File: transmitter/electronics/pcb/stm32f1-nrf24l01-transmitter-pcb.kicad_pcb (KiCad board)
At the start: 2 copper layers, 100 x 48 mm, 69 parts, among them J1 PA1/A1, J10 PB3, J11 PB4, J12 PB5, J13 PB6, J14 PB7, J15 PB8, J16 PB10, J17 PB11, J18 External charger LED, J19 BATTERY, J2 PA2/A2, J20 Red, J21 Blue, J22 POWER SWITCH, J23 USB, J24 UART, J25 SWD, J26 Buzzer, J27 NRF24 connector, J29 Meter, J3 PA3/A3, J30 LED, J4 PA4/A4, J5 PA5/A5, J6 PA6/A6, J7 PA7/A7, J8 PB0/A8, J9 PB1/A9, Q1 PMV30UN, SW1 RESET, U1 MCP1703A-3302, U2 LIPO_CHARGER_+_PROTECTION, U3 STM32F103CBT6, U4 MCP1703A-3302, Y1 8MHz

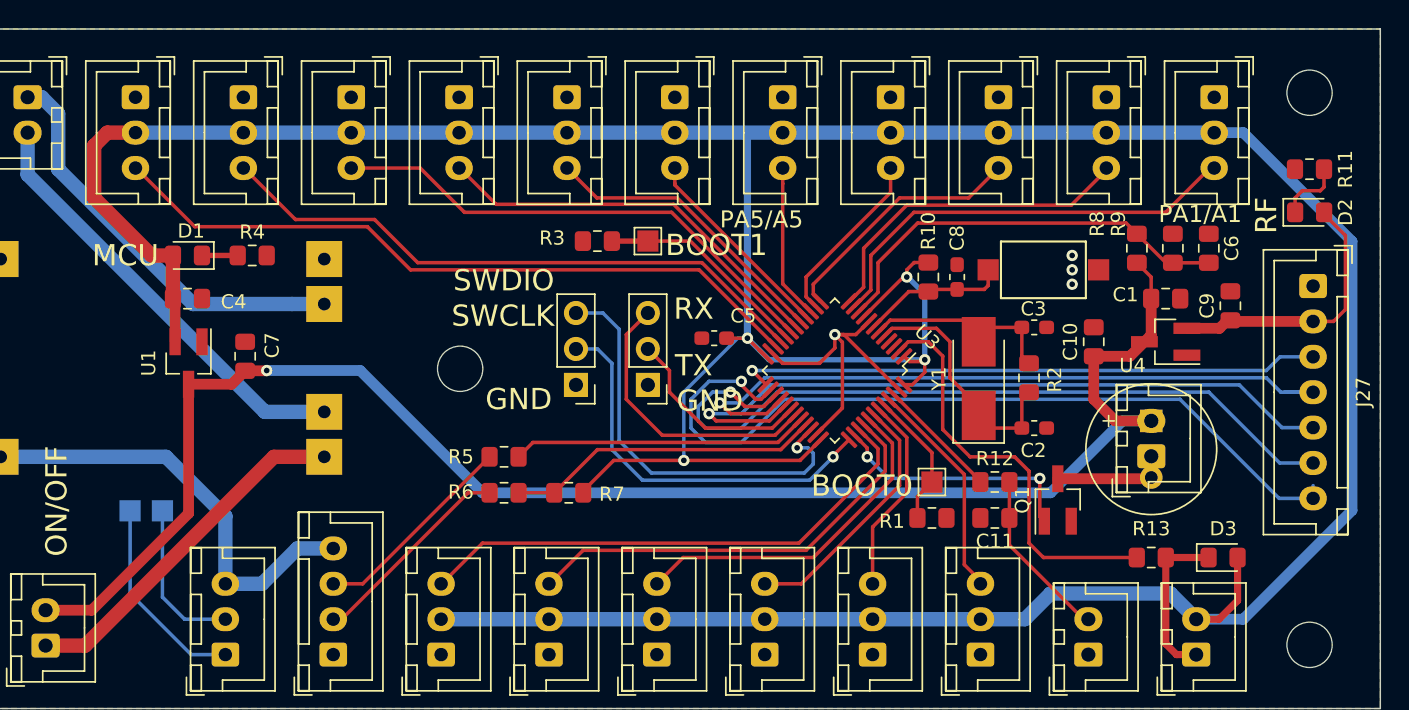
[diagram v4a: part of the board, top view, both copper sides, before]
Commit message: Revise layout
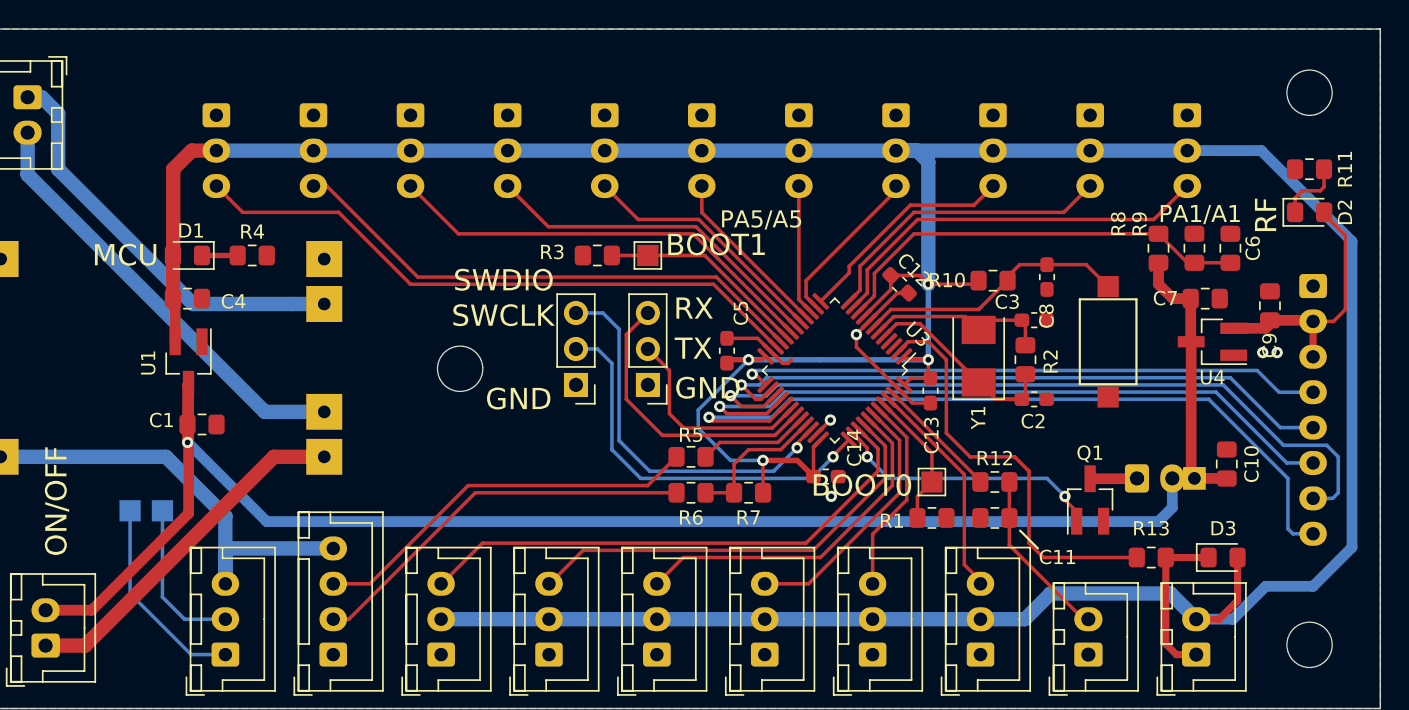
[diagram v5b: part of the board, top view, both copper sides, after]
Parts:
- added C12: 100n, Capacitor_SMD:C_0603_1608Metric_Pad1.05x0.95mm_HandSolder, F.Cu at (166.0, 70.0)
- added C13: 100n, Capacitor_SMD:C_0603_1608Metric_Pad1.05x0.95mm_HandSolder, F.Cu at (168.2, 77.5)
- added C14: 100n, Capacitor_SMD:C_0603_1608Metric_Pad1.05x0.95mm_HandSolder, F.Cu at (160.8, 83.6)
- J1, J16, J17, J2, J26, J3, J4, J5, J6, J7, J8, J9, SP1: moved to B.Cu
- J27: footprint Connector_JST:JST_XH_B7B-XH-A_1x07_P2.50mm_Vertical -> Connector_JST:JST_XH_B8B-XH-A_1x08_P2.50mm_Vertical; moved to B.Cu
- Y1: footprint Crystal:Crystal_SMD_5032-2Pin_5.0x3.2mm_HandSoldering -> Crystal:Crystal_SMD_5032-2Pin_5.0x3.2mm
- moved C1 68.7 mm to (116.8, 79.9)
- moved C7 67.9 mm to (187.6, 71.0), turned to 0 degrees
- moved R5 13.2 mm to (151.3, 82.2)
- moved R6 13.2 mm to (151.3, 84.8)
- moved C10 12.8 mm to (189.2, 82.7)
- moved R7 12.7 mm to (155.4, 84.8)
- moved SW1 6.83 mm to (180.8, 74.1), turned to 90 degrees
- moved C8 6.35 mm to (176.5, 69.5), turned to 270 degrees
- moved J17 5.85 mm to (117.8, 58.1)
- moved J16 5.11 mm to (124.6, 58.1)
- moved SP1 5.08 mm to (186.9, 83.7), turned to 180 degrees
- moved R10 4.58 mm to (172.6, 69.8), turned to 0 degrees
- moved J9 4.38 mm to (131.5, 58.1)
- moved J8 3.66 mm to (138.4, 58.1)
- moved U4 3.30 mm to (188.1, 74.1)
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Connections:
- J27 pad 3: /CSN -> /3V3_RF
- J27 pad 4: /MOSI -> /CSN
- J27 pad 5: /IRQ -> /SCK
- J27 pad 6: /MISO -> /MOSI
- J27 pad 7: /SCK -> /MISO
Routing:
- net +3V3: track 281.4 -> 263.9 mm
- net /SCK: track 58.9 -> 44.8 mm
- net /USBDM: track 21.0 -> 7.81 mm
- net Net-(J23-Pad2): track 14.7 -> 27.9 mm
- net Net-(J23-Pad3): track 14.8 -> 28.0 mm
- net /USBDP: track 22.3 -> 10.3 mm
- net /NRST: track 10.4 -> 19.1 mm
- net VDD: track 114.1 -> 122.1 mm
- net /PB11: track 50.4 -> 44.2 mm
- net /PB10: track 43.0 -> 37.5 mm
- net Net-(J26-Pad1): track 8.14 -> 3.38 mm
- net /PB1-ADC9: track 35.8 -> 31.1 mm
- net /IRQ: track 50.9 -> 55.2 mm
- net /PB0-ADC8: track 28.4 -> 24.5 mm
- net GND: track 23.3 -> 19.7 mm, vias 4 -> 5
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
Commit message: Make combined PCB
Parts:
- added H4: MountingHole, MountingHole:MountingHole_3.2mm_M3_DIN965, F.Cu at (140.0, 91.0)
- added H5: MountingHole, MountingHole:MountingHole_3.2mm_M3_DIN965, F.Cu at (140.0, 63.0)
- added H6: MountingHole, MountingHole:MountingHole_3.2mm_M3_DIN965, F.Cu at (195.0, 63.0)
- added H7: MountingHole, MountingHole:MountingHole_3.2mm_M3_DIN965, F.Cu at (195.0, 91.0)
- added H8: MountingHole, MountingHole:MountingHole_3.2mm_M3_DIN965, F.Cu at (100.0, 63.0)
- J10, J11, J12, J13, J14, J15, J18, J19, J22, J23, J29, J30: moved to B.Cu
- moved R7 41.8 mm to (114.7, 94.4)
- moved R5 38.6 mm to (112.7, 82.5)
- moved R6 38.6 mm to (112.7, 84.8)
- moved J18 34.7 mm to (83.7, 95.4), turned to 180 degrees
- moved R4 34.0 mm to (89.1, 81.5), turned to 270 degrees
- moved J20 33.1 mm to (81.2, 90.9)
- moved J16 32.4 mm to (92.6, 63.4)
- moved J17 32.4 mm to (85.8, 63.4)
- moved D1 28.3 mm to (89.1, 77.4), turned to 90 degrees
- moved J25 27.5 mm to (120.1, 92.1)
- moved J21 27.1 mm to (85.0, 90.9)
- moved J19 26.4 mm to (78.9, 63.4)
- moved TP2 25.4 mm to (123.0, 70.4), turned to 90 degrees
- moved U2 25.4 mm to (89.1, 80.2)
- moved R3 25.0 mm to (119.8, 70.4)
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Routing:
- net /USBDP: track 10.3 -> 42.0 mm
- net /USBDM: track 7.81 -> 32.7 mm
- net Net-(J23-Pad2): track 27.9 -> 10.4 mm
- net Net-(J23-Pad3): track 28.0 -> 10.9 mm
- net /PB11: track 44.2 -> 61.0 mm
- net /PB10: track 37.5 -> 54.3 mm
- net /METER: track 8.69 -> 24.1 mm
- net /PA2-ADC2: track 21.4 -> 36.2 mm
- net +3V3: track 263.9 -> 278.7 mm, vias 4 -> 1
- net /PA3-ADC3: track 15.8 -> 30.3 mm
- net /PA4-ADC4: track 11.4 -> 25.8 mm
- net /PB5: track 24.8 -> 10.4 mm
- net /PA1-ADC1: track 28.0 -> 42.4 mm
- net VDD: track 122.1 -> 134.8 mm, vias 1 -> 2
- net /PA5-ADC5: track 9.20 -> 20.1 mm
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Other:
- board size 100 x 48 mm -> 124 x 47 mm
- net class Default: clearance 0.2 -> 0.2032; trace_width 0.25 -> 0.254
- rule trace_clearance: 0.2 -> 0.2032
- rule trace_min: 0.2 -> 0.2032
- board text added: "+ DM DP GND"
- board text added: "- +"
- board text added: "3V3 MCU"
- board text added: "3V3 RF"
- board text added: "B+"
- board text added: "B-"
- board text added: "BAT"
- board text added: "BATTERY"
- board text added: "BUZZER"
- board text added: "CHARGER LED"
- board text added: "LED"
- board text added: "METER"
- board text added: "NRF24L01P"
- board text added: "OUT+"
- board text added: "OUT-"
- board text added: "PA2/A2"
- board text added: "PA3/A3"
- board text added: "PA4/A4"
- board text added: "PA6/A6"
- board text added: "PA7/A7"
- board text added: "PB0/A8"
- board text added: "PB1/A9"
- board text added: "PB10"
- board text added: "PB11"
- board text added: "PB3"
- board text added: "PB4"
- board text added: "PB5"
- board text added: "PB6"
- board text added: "PB7"
- board text added: "PB8"
- board text added: "RESET"
- board text added: "USB"
- board text removed: "MCU"
- board text removed: "RF"

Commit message: Finalize layout
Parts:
- added H10: MountingHole, MountingHole:MountingHole_3.2mm_M3_DIN965, F.Cu at (75.0, 56.5)
- added H9: MountingHole, MountingHole:MountingHole_3.2mm_M3_DIN965, F.Cu at (75.0, 95.5)
- H4, H5, H6, H7, H8: footprint MountingHole:MountingHole_3.2mm_M3_DIN965 -> MountingHole:MountingHole_2.7mm_M2.5_DIN965
- moved J9 35.1 mm to (90.9, 63.4)
- moved J19 28.7 mm to (103.0, 78.9)
- moved J22 28.4 mm to (103.0, 70.0), turned to 270 degrees
- moved R7 8.75 mm to (106.9, 90.6), turned to 0 degrees
- moved J16 8.64 mm to (84.0, 63.4)
- moved J17 8.64 mm to (77.1, 63.4)
- moved C1 7.27 mm to (92.1, 78.2), turned to 90 degrees
- moved J25 7.23 mm to (113.2, 89.8), turned to 90 degrees
- moved R5 6.84 mm to (106.9, 86.0)
- moved R6 6.84 mm to (106.9, 88.3)
- moved J23 6.78 mm to (102.0, 94.9), turned to 180 degrees
- moved D1 5.24 mm to (85.0, 74.1)
- moved U1 5.24 mm to (88.6, 77.6)
- moved R4 5.24 mm to (85.0, 78.2)
- moved C4 5.24 mm to (88.6, 73.1)
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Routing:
- net /PB1-ADC9: track 21.5 -> 57.2 mm
- net Net-(J19-Pad2): track 31.4 -> 7.67 mm
- net Net-(J19-Pad1): track 30.3 -> 7.66 mm
- net +3V3: track 278.7 -> 294.7 mm
- net /+USB: track 40.9 -> 25.9 mm
- net /RX: track 27.0 -> 14.9 mm
- net /PB10: track 54.3 -> 65.9 mm
- net /PB11: track 61.0 -> 72.6 mm
- net Net-(J22-Pad1): track 14.8 -> 25.0 mm
- net /USBDM: track 32.7 -> 38.3 mm
- net VDD: track 134.8 -> 129.5 mm
- net /SWDCLK: track 33.0 -> 38.1 mm
- net /TX: track 23.0 -> 18.0 mm
- net Net-(J23-Pad3): track 10.9 -> 14.5 mm
- net /SWDIO: track 26.3 -> 29.5 mm
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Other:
- board size 124 x 47 mm -> 128 x 47 mm
- net class Default: clearance 0.2032 -> 0.1524
- rule trace_clearance: 0.2032 -> 0.1524
- board text added: "+"
- board text added: "LANE Boys RC"

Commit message: Add JLC fabrication marker
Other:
- board text added: "JLCJLCJLCJLC"
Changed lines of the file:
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@@
   (general
     (thickness 1.6)
-    (drawings 99)
+    (drawings 100)
     (tracks 406)
     (zones 0)
@@
   )
   (setup
-    (last_trace_width 0.381)
+    (last_trace_width 0.254)
     (user_trace_width 0.381)
     (user_trace_width 0.508)
@@
     (pad_drill 3.2)
     (pad_to_mask_clearance 0)
-    (aux_axis_origin 100 100)
-    (grid_origin 100 100)
+    (aux_axis_origin 71 100)
+    (grid_origin 71 100)
     (visible_elements FFFFFF7F)
     (pcbplotparams
@@
     )
   )
+  (gr_text JLCJLCJLCJLC (at 73.584 80.188 90) (layer B.SilkS)
+    (effects (font (size 0.8 0.8) (thickness 0.15)) (justify mirror))
+  )
   (gr_text + (at 191.948 81.458 90) (layer F.SilkS)
     (effects (font (size 1.5 1.5) (thickness 0.3)) (justify left))
@@
   (segment (start 99.532 94.92) (end 99.532 90.054) (width 0.254) (layer F.Cu) (net 36))
   (segment (start 99.532 90.054) (end 101.27 88.316) (width 0.254) (layer F.Cu) (net 36))
+  (segment (start 105.851 88.0575) (end 105.851 88.316) (width 0.254) (layer F.Cu) (net 36))
+  (segment (start 103.801 88.316) (end 105.833 88.316) (width 0.254) (layer F.Cu) (net 36))
   (segment (start 131.496 84.506) (end 130.48 83.49) (width 0.254) (layer F.Cu) (net 37) (status 20))
   (segment (start 144.223445 82.800109) (end 142.517554 84.506) (width 0.254) (layer F.Cu) (net 37) (status 10))
@@
   (segment (start 145.284105 83.860769) (end 143.114874 86.03) (width 0.254) (layer F.Cu) (net 39) (status 10))
   (segment (start 143.114874 86.03) (end 122.098 86.03) (width 0.254) (layer F.Cu) (net 39))
+  (segment (start 117.272 91.364) (end 115.748 89.84) (width 0.254) (layer F.Cu) (net 40))
+  (segment (start 119.05 91.364) (end 117.272 91.364) (width 0.254) (layer F.Cu) (net 40))
+  (segment (start 123.876 86.538) (end 119.05 91.364) (width 0.254) (layer F.Cu) (net 40))
+  (segment (start 147.498 85.058664) (end 147.498 87.3) (width 0.254) (layer F.Cu) (net 40))
+  (segment (start 142.926 86.538) (end 123.876 86.538) (width 0.254) (layer F.Cu) (net 40))
+  (segment (start 147.988788 84.567876) (end 147.498 85.058664) (width 0.254) (layer F.Cu) (net 40))
+  (segment (start 147.498 87.3) (end 146.99 87.808) (width 0.254) (layer F.Cu) (net 40))
+  (segment (start 146.99 87.808) (end 144.196 87.808) (width 0.254) (layer F.Cu) (net 40))
+  (segment (start 144.196 87.808) (end 142.926 86.538) (width 0.254) (layer F.Cu) (net 40))
   (segment (start 175.224 82.752) (end 175.248 82.728) (width 0.762) (layer F.Cu) (net 41) (status 30))
   (segment (start 175.248 82.728) (end 176.708 82.728) (width 0.762) (layer F.Cu) (net 41) (status 30))
@@
   (segment (start 144.576998 83.153662) (end 143.32933 84.40133) (width 0.254) (layer F.Cu) (net 50) (status 10))
   (segment (start 143.32933 84.40133) (end 142.71666 85.014) (width 0.254) (layer F.Cu) (net 50))
-  (segment (start 105.851 88.0575) (end 105.851 88.316) (width 0.254) (layer F.Cu) (net 36))
-  (segment (start 103.801 88.316) (end 105.833 88.316) (width 0.254) (layer F.Cu) (net 36))
-  (segment (start 117.272 91.364) (end 115.748 89.84) (width 0.254) (layer F.Cu) (net 40))
-  (segment (start 119.05 91.364) (end 117.272 91.364) (width 0.254) (layer F.Cu) (net 40))
-  (segment (start 123.876 86.538) (end 119.05 91.364) (width 0.254) (layer F.Cu) (net 40))
-  (segment (start 147.498 85.058664) (end 147.498 87.3) (width 0.254) (layer F.Cu) (net 40))
-  (segment (start 142.926 86.538) (end 123.876 86.538) (width 0.254) (layer F.Cu) (net 40))
-  (segment (start 147.988788 84.567876) (end 147.498 85.058664) (width 0.254) (layer F.Cu) (net 40))
-  (segment (start 147.498 87.3) (end 146.99 87.808) (width 0.254) (layer F.Cu) (net 40))
-  (segment (start 146.99 87.808) (end 144.196 87.808) (width 0.254) (layer F.Cu) (net 40))
-  (segment (start 144.196 87.808) (end 142.926 86.538) (width 0.254) (layer F.Cu) (net 40))
   (segment (start 120.828 85.014) (end 120.574 85.014) (width 0.254) (layer F.Cu) (net 50))
   (segment (start 142.71666 85.014) (end 120.828 85.014) (width 0.254) (layer F.Cu) (net 50))
